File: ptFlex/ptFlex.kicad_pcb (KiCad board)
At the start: 2 copper layers, 50 x 100 mm, 72 parts, among them J1 Barrel_Jack_Switch, J2 Programming, J3 Qwiic, J4 6 Pin Male Header, Q1 MMBT3904, Q2 MMBT3904, Q3 DMP2004K-7, Q4 BSS138, Q5 BSS138, U1 LM1086-5.0, U2 LP3985IM5-3.3/NOPB, U3 ATMega 328p-AU, U4 ATGM336H-5N31, U5 SA818S-V, U6 BME280, Y1 16MHz

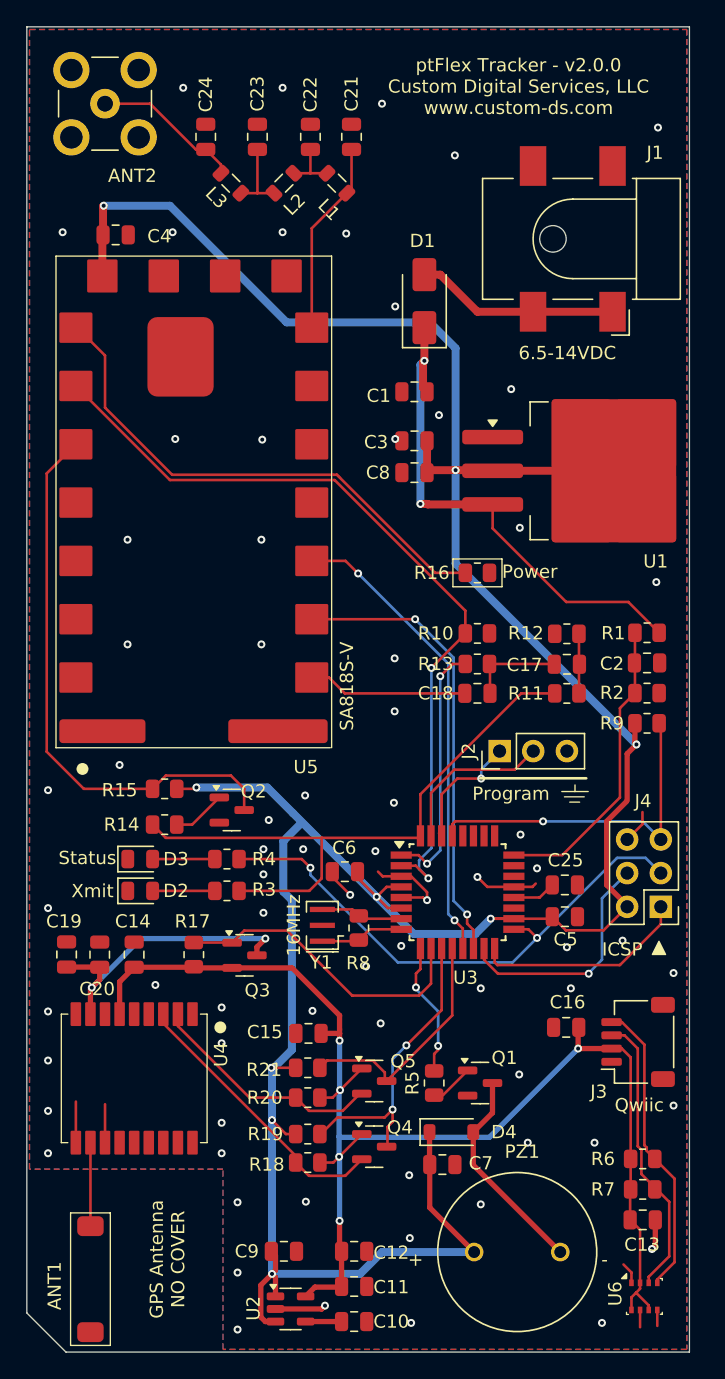
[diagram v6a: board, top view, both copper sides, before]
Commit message: Board redesigned to 2.0.1 to fix missing SDA/SCL pins to uC. Shrunk board slightly. Fixed SMA center hole being too small.
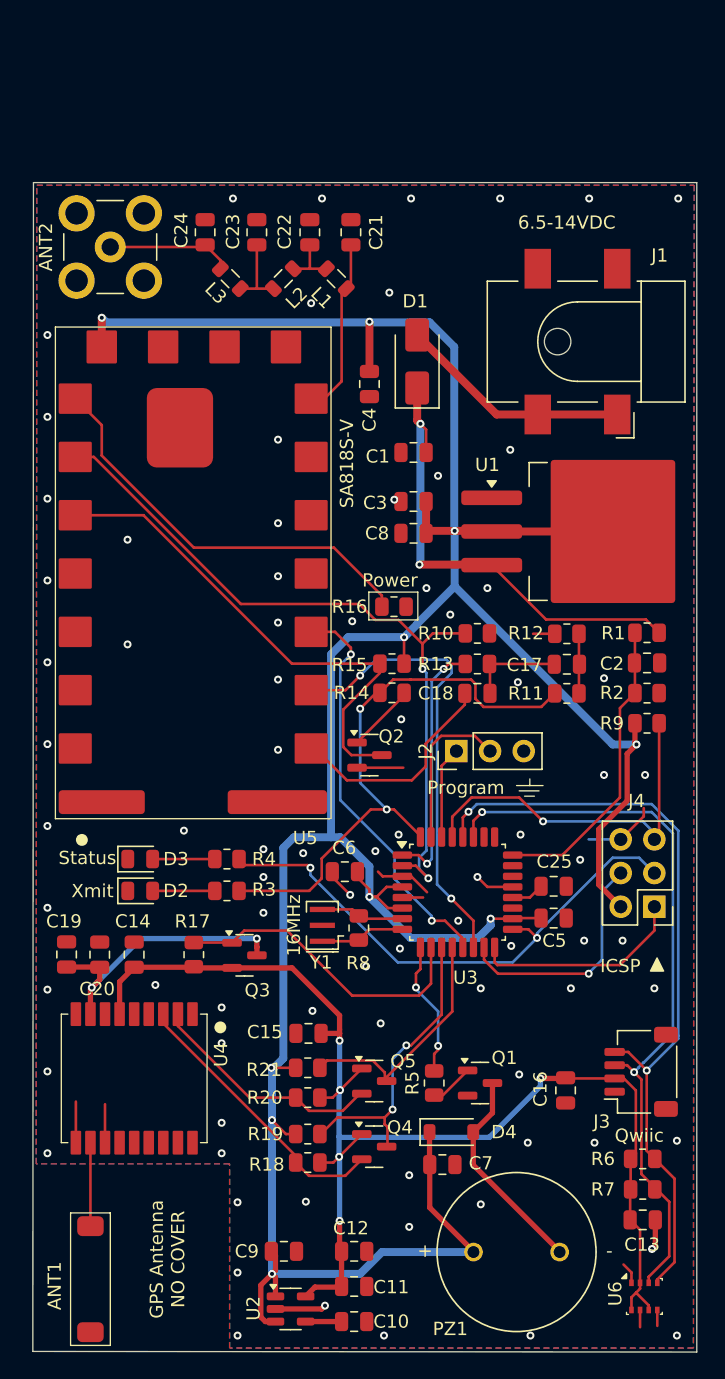
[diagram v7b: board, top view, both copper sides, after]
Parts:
- ANT2: footprint Connector_Coaxial:SMB_Jack_Vertical -> Custom DS:SMA_Thru_Hole
- PZ1: footprint Piezo - CEM-1206S:CUI_CEM-1206S -> Custom DS:CUI_CEM-1206S
- moved C4 22.2 mm to (141.7, 72.8), turned to -90 degrees
- moved R14 19.8 mm to (143.4, 96.1)
- moved R15 19.6 mm to (143.4, 93.9)
- moved Q2 11.2 mm to (141.7, 100.8)
- moved ANT2 10.8 mm to (122.1, 62.5)
- moved J1 7.76 mm to (157.4, 69.6)
- moved C21 7.20 mm to (140.3, 61.4)
- moved C22 7.20 mm to (137.2, 61.4)
- moved C23 7.20 mm to (133.2, 61.4)
- moved C24 7.20 mm to (129.3, 61.4)
- moved L1 7.20 mm to (139.2, 64.8)
- moved L2 7.20 mm to (135.2, 64.8)
- moved L3 7.20 mm to (131.2, 64.8)
- moved R16 6.79 mm to (143.6, 89.6)
- moved U5 5.35 mm to (129.0, 88.3)
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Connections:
- J3 pad 3: Net-(J3-Pin_3) -> SDA
- J3 pad 4: Net-(J3-Pin_4) -> SCL
- R6 pad 2: Net-(J3-Pin_4) -> SCL
- R7 pad 2: Net-(J3-Pin_3) -> SDA
- U6 pad 3: Net-(J3-Pin_3) -> SDA
- U6 pad 4: Net-(J3-Pin_4) -> SCL
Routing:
- net SCL: track 0.00 -> 58.8 mm, vias 0 -> 2
- net SDA: track 0.00 -> 55.7 mm, vias 0 -> 2
- net Net-(J3-Pin_4): track 23.0 -> 0.00 mm
- net Net-(J3-Pin_3): track 21.7 -> 0.00 mm
- net Net-(U5-HIGH/LOW): track 39.4 -> 31.5 mm
- net +5V: track 227.3 -> 234.5 mm, vias 9 -> 10
- net GND: track 32.9 -> 38.3 mm, vias 72 -> 82
- net Net-(U5-MIC-IN): track 12.0 -> 17.2 mm
- net XMIT-TX: track 35.5 -> 30.9 mm
- net Net-(Q2-C): track 42.6 -> 38.2 mm
- net XMIT-POWERSAVE: track 60.8 -> 56.5 mm
- net +3.3V: track 103.1 -> 99.0 mm
- net Net-(D1-K): track 39.0 -> 36.0 mm
- net XMIT-PTT: track 46.8 -> 44.1 mm, vias 0 -> 2
- net Net-(J2-Pin_1): track 9.55 -> 7.14 mm, vias 1 -> 0
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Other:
- board size 50 x 100 mm -> 50.1 x 88.2 mm
- board text added: "ptFlex Tracker - v2.0.1 Custom Digital Services, LLC www.custom-ds.com"
- board text removed: "ptFlex Tracker - v2.0.0 Custom Digital Services, LLC www.custom-ds.com"
